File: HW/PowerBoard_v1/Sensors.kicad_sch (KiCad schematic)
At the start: 4 parts, among them U1 AMC130M02DFMR, U1 MCP9700AT-ETT, U5 AMC130M02DFMR

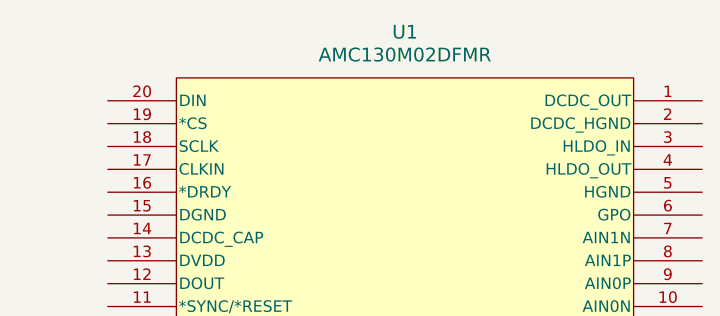
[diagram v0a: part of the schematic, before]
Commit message: cleaned up schematic
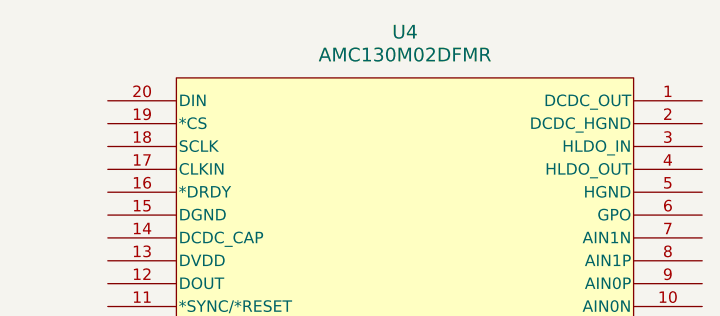
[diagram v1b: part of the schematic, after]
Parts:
- renumbered U1 to U4
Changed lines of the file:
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@@
         )
         (path "/1e1b062d-fad0-427c-a622-c5b8a80b5268/f37b00a5-62bb-47d6-b18e-0a47b6349fc3"
-          (reference "#PWR03") (unit 1)
+          (reference "#PWR017") (unit 1)
         )
       )
@@
         )
         (path "/1e1b062d-fad0-427c-a622-c5b8a80b5268/f37b00a5-62bb-47d6-b18e-0a47b6349fc3"
-          (reference "U4") (unit 1)
+          (reference "U3") (unit 1)
         )
       )
@@
   (symbol (lib_id "AMC130M02DFMR:AMC130M02DFMR") (at 109.22 43.18 0) (unit 1)
     (in_bom yes) (on_board yes) (dnp no) (fields_autoplaced)
-    (property "Reference" "U1" (at 140.97 31.75 0)
+    (property "Reference" "U4" (at 140.97 31.75 0)
       (effects (font (size 1.524 1.524)))
     )
@@
       (project "power_v1"
         (path "/1e1b062d-fad0-427c-a622-c5b8a80b5268/f37b00a5-62bb-47d6-b18e-0a47b6349fc3"
-          (reference "U1") (unit 1)
+          (reference "U4") (unit 1)
         )
       )
@@
         )
         (path "/1e1b062d-fad0-427c-a622-c5b8a80b5268/f37b00a5-62bb-47d6-b18e-0a47b6349fc3"
-          (reference "#PWR04") (unit 1)
+          (reference "#PWR018") (unit 1)
         )
       )
@@
         )
         (path "/1e1b062d-fad0-427c-a622-c5b8a80b5268/f37b00a5-62bb-47d6-b18e-0a47b6349fc3"
-          (reference "C10") (unit 1)
+          (reference "C9") (unit 1)
         )
       )

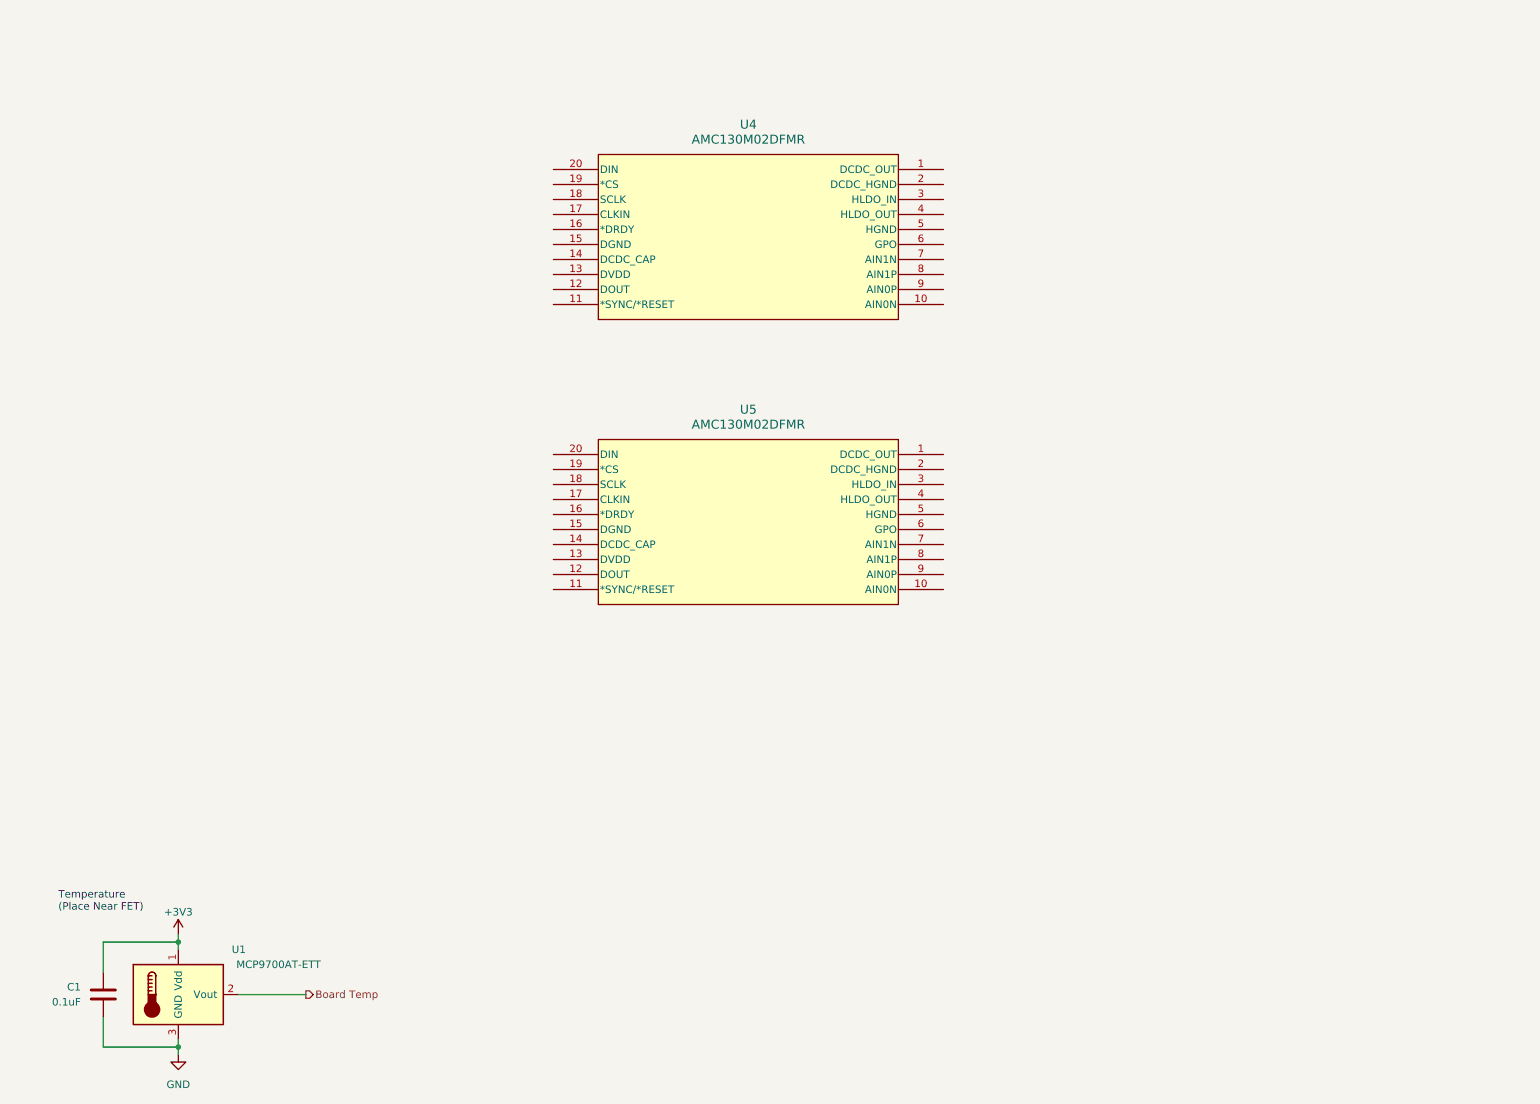
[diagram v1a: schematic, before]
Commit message: update sim to simulate array better
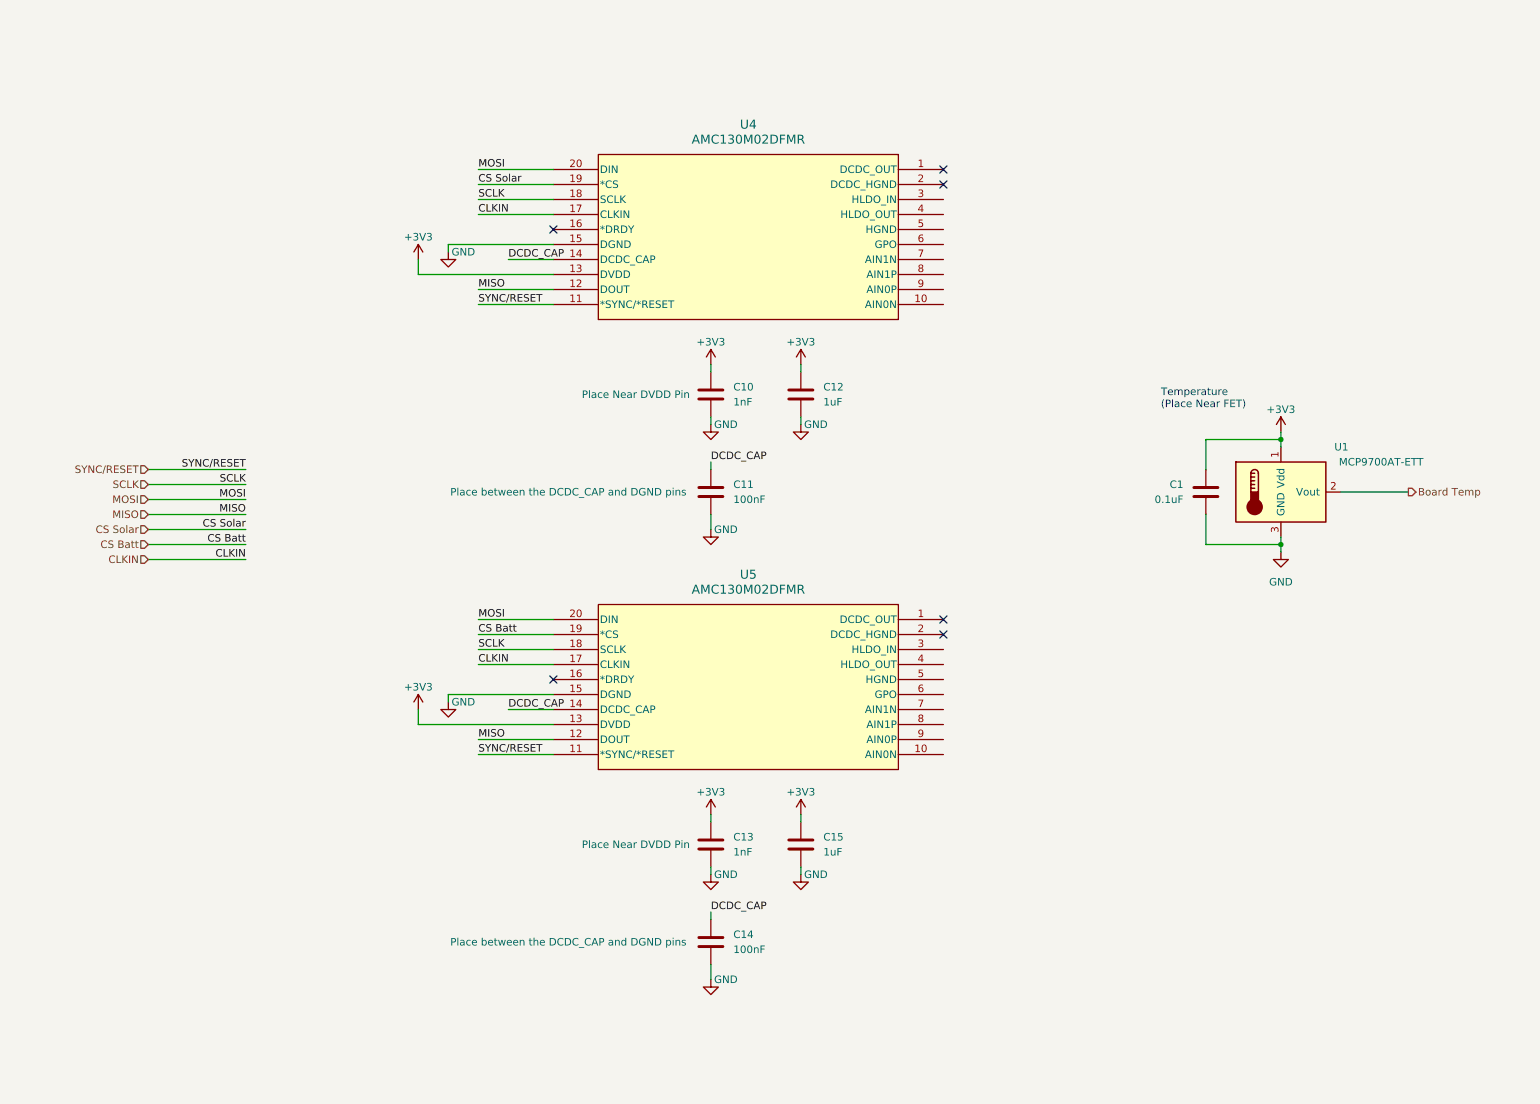
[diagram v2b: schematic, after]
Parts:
- added C10, C13: 1nF, symbol Device:C
- added C11, C14: 100nF, symbol Device:C
- added C12, C15: 1uF, symbol Device:C
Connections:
- net +3V3: now also U4.13 (DVDD), U5.13 (DVDD), C10.1, C12.1, C13.1, C15.1
- net GND: now also U4.15 (DGND), U5.15 (DGND), C10.2, C11.2, C12.2, C13.2, C14.2, C15.2
- net SYNC/RESET: now reaches U4.11 (*SYNC/*RESET)
- net SYNC/RESET: now also U5.11 (*SYNC/*RESET)
- net MISO: now reaches U4.12 (DOUT)
- net MISO: now also U5.12 (DOUT)
- net DCDC_CAP: now reaches U4.14 (DCDC_CAP)
- net DCDC_CAP: now also U5.14 (DCDC_CAP), C11.1, C14.1
- net CLKIN: now reaches U4.17 (CLKIN)
- net CLKIN: now also U5.17 (CLKIN)
- net SCLK: now reaches U4.18 (SCLK)
- net SCLK: now also U5.18 (SCLK)
- net CS Solar: now reaches U4.19 (*CS)
- net MOSI: now reaches U4.20 (DIN)
- net MOSI: now also U5.20 (DIN)
- net CS Batt: now reaches U5.19 (*CS)
- no-connect marks 0 -> 6
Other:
- moved on the sheet: C1, U1

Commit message: updates sensing
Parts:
- removed C10, C13: 1nF, symbol Device:C
- removed C11, C14: 100nF, symbol Device:C
- removed C12, C15: 1uF, symbol Device:C
- removed U4, U5: AMC130M02DFMR, SOIC20_DFM_TEX, symbol AMC130M02DFMR:AMC130M02DFMR
- added U4: PAMC1350DWVR, U_PAMC1350DWVR_TEX, symbol AMC1350:PAMC1350DWVR
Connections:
- no-connect marks 6 -> 0

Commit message: updated sensing portion
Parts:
- added C10, C11, C15, C16, C20, C21, C22, C23: 100nF, Capacitor_SMD:C_0603_1608Metric_Pad1.08x0.95mm_HandSolder, symbol device:C
- added C12, C13, C14, C17, C18, C19, C24, C25: 1uF, Capacitor_SMD:C_0603_1608Metric_Pad1.08x0.95mm_HandSolder, symbol device:C
- added C26: 10uF, Capacitor_SMD:C_0603_1608Metric_Pad1.08x0.95mm_HandSolder, symbol device:C
- added C27: 2.2nF, Capacitor_SMD:C_0603_1608Metric_Pad1.08x0.95mm_HandSolder, symbol device:C
- added C28: 1nF, Capacitor_SMD:C_0603_1608Metric_Pad1.08x0.95mm_HandSolder, symbol device:C
- added L3: 22uH, Inductor_SMD:L_0603_1608Metric_Pad1.05x0.95mm_HandSolder, symbol device:L
- added TP1: +3V3A, TestPoint:TestPoint_THTPad_1.0x1.0mm_Drill0.5mm, symbol Connector:TestPoint
- added TP2: GNDA, TestPoint:TestPoint_THTPad_1.0x1.0mm_Drill0.5mm, symbol Connector:TestPoint
- added U5, U6, U7: PAMC1350DWVR, U_PAMC1350DWVR_TEX, symbol AMC1350:PAMC1350DWVR
- added U8: 3v3 ISO DC/DC, Converter_DCDC:Converter_DCDC_RECOM_R-78S-0.1_THT, symbol Regulator_Switching:CRE1S0305S3C
- U4: MPN (none) -> PAMC1350DWVR
- renumbered C1 to C9, U1 to U3
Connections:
- net +3V3: now also U4.8 (VDD2), C10.1, C12.1, C16.1, C17.1, C22.1, C23.1, C24.1, C25.1, C26.1, L3.1, U5.8 (VDD2), U6.8 (VDD2), U7.8 (VDD2)
- net GND: now also U4.5 (GND2), U4.6 (OUTN), C10.2, C12.2, C16.2, C17.2, C22.2, C23.2, C24.2, C25.2, C26.2, C27.1, U5.5 (GND2), U5.6 (OUTN), U6.5 (GND2), U6.6 (OUTN), U7.5 (GND2), U7.6 (OUTN), U8.1 (-VIN)
- net +3.3VA: now reaches U4.1 (VDD1)
- net +3.3VA: now also C11.1, C13.1, C14.1, C15.1, C18.1, C19.1, C20.1, C21.1, C28.1, TP1.1, U5.1 (VDD1), U6.1 (VDD1), U7.1 (VDD1), U8.4 (+VOUT)
- net V Sense Sol: now reaches U4.2 (INP)
- net Earth: now reaches U4.3 (INN)
- net Earth: now also U4.4 (GND1), C11.2, C13.2, C14.2, C15.2, C18.2, C19.2, C20.2, C21.2, C27.2, TP2.1, U5.3 (INN), U5.4 (GND1), U6.4 (GND1), U7.4 (GND1), U8.3 (-VOUT)
- net ADC V Sol: now reaches U4.7 (OUTP)
- new net: C28.2, L3.2, U8.2 (+VIN)
- new net ADC I Batt: U7.7 (OUTP)
- new net ADC I Sol: U6.7 (OUTP)
- new net ADC V Batt: U5.7 (OUTP)
- new net I+ Sense Batt: U7.2 (INP)
- new net I+ Sense Sol: U6.2 (INP)
- new net I- Sense Batt: U7.3 (INN)
- new net I- Sense Sol: U6.3 (INN)
- new net V Sense Batt: U5.2 (INP)
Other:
- note added: "+3.3VA represents the High Voltage 3.3v side."
- note added: "HV Side"
- note added: "LV Side"
- moved on the sheet: C9, U3, U4

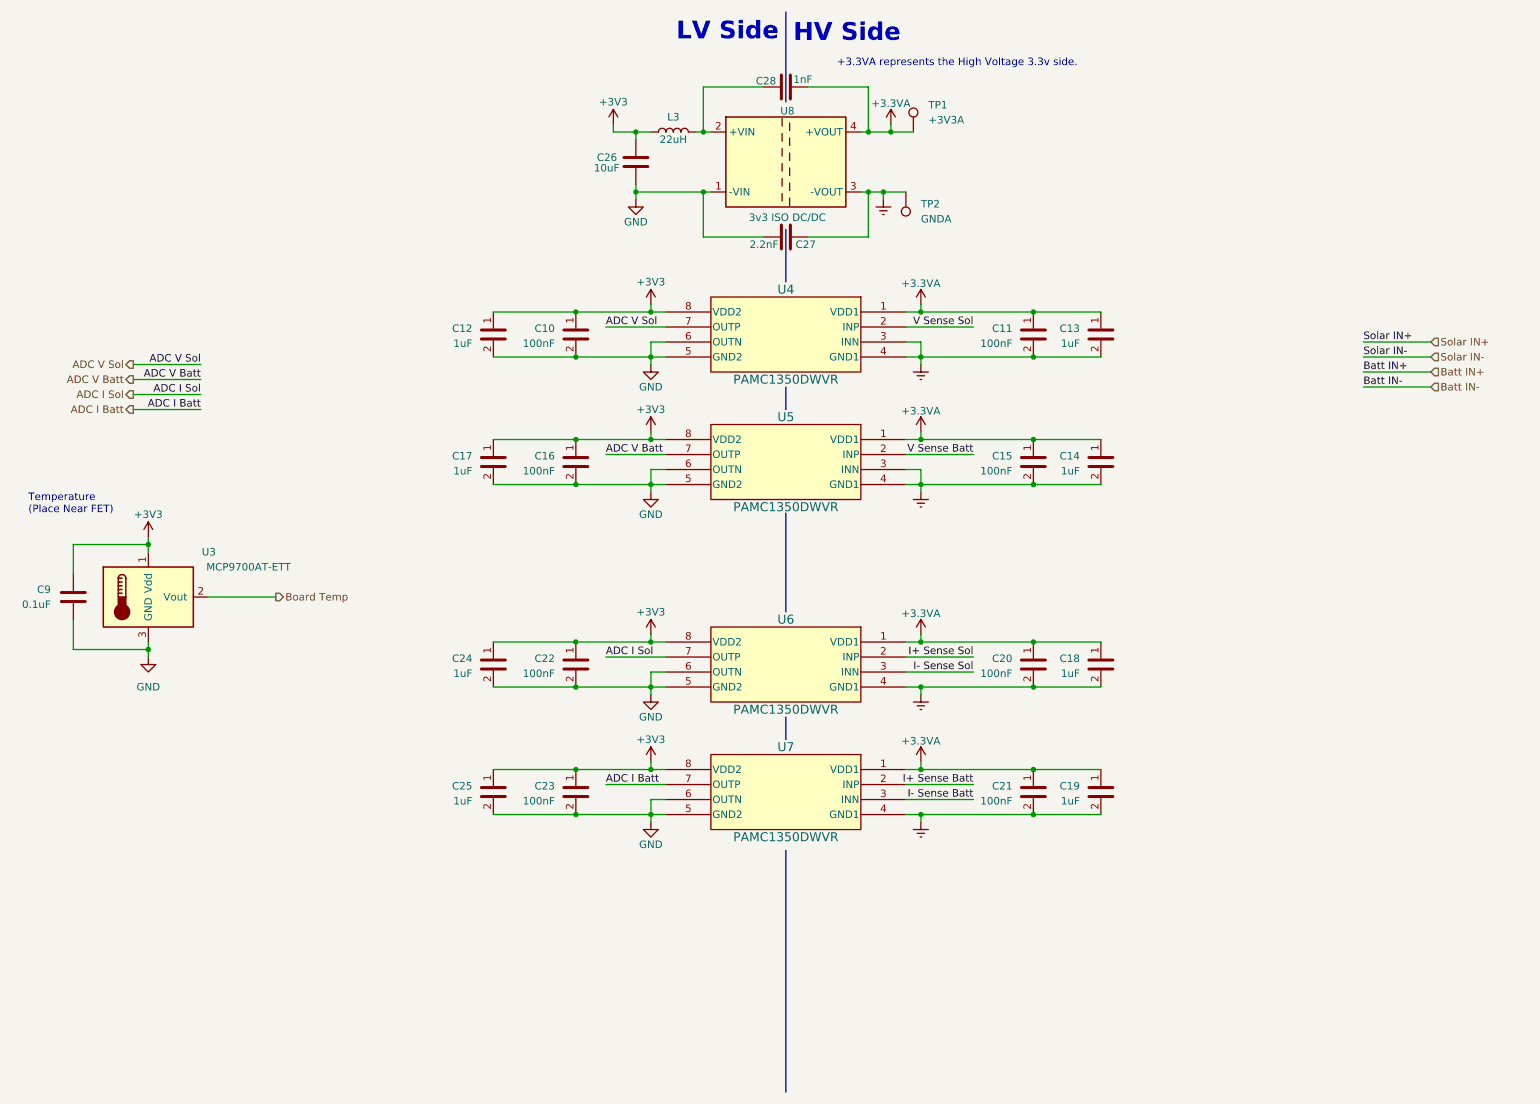
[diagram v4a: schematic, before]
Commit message: added resistors for sensing
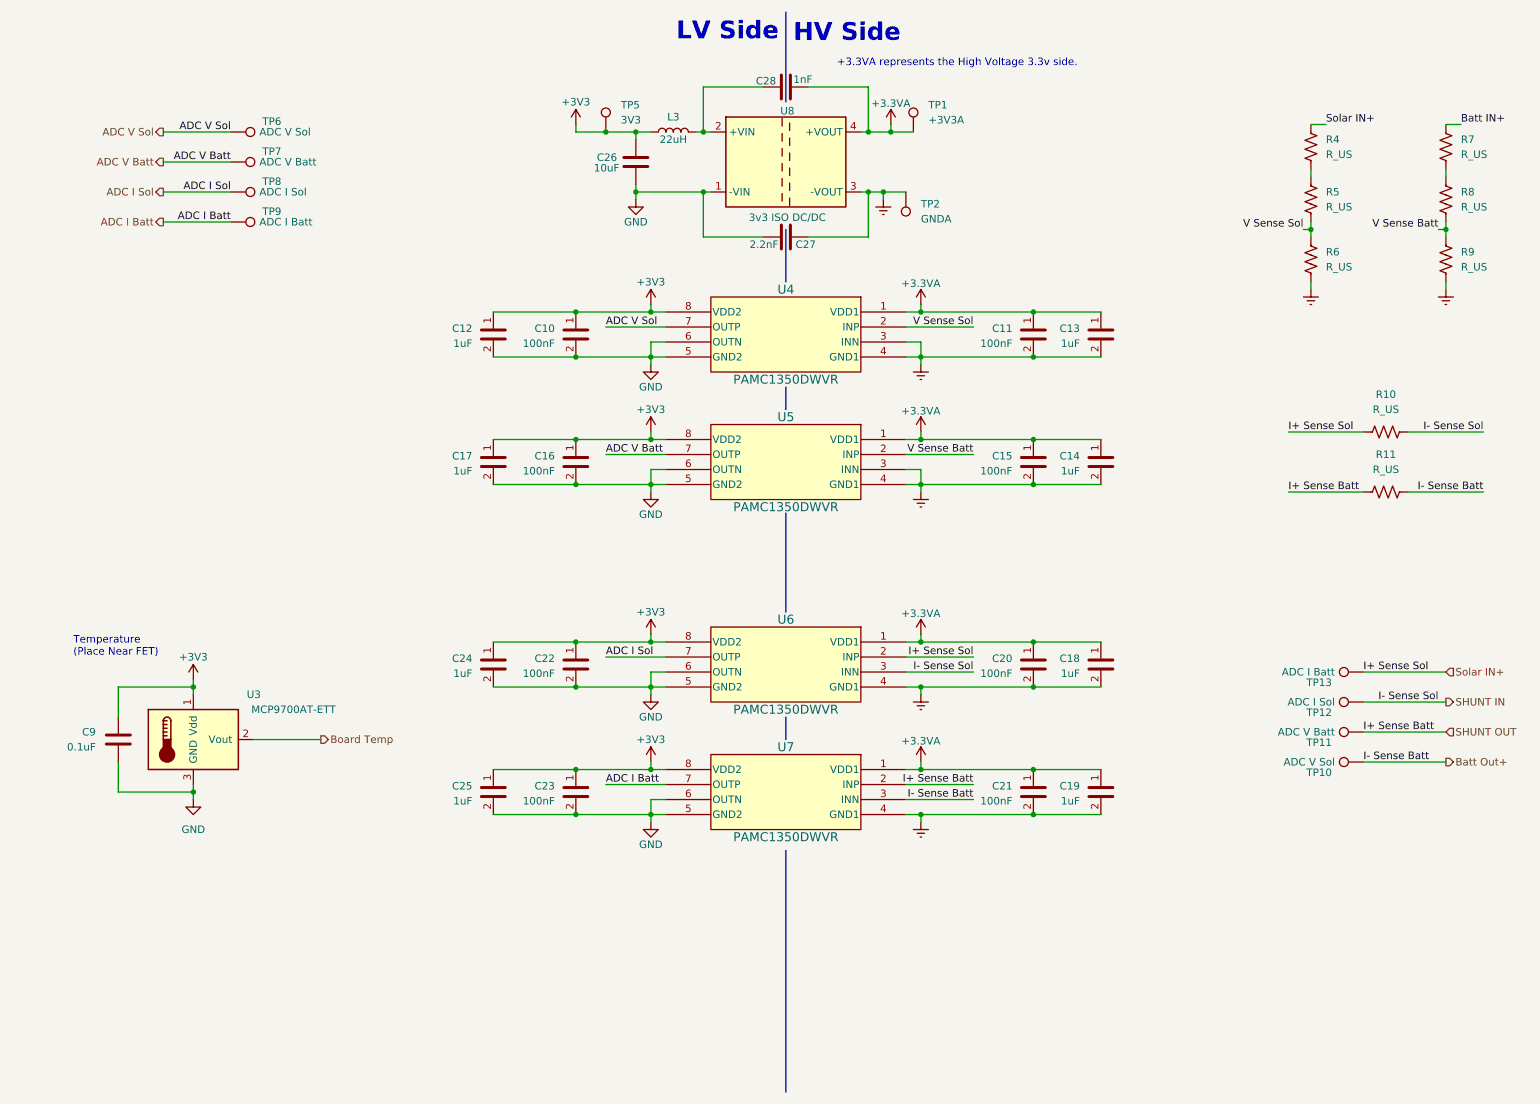
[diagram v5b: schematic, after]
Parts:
- added R10, R11, R4, R5, R6, R7, R8, R9: R_US, symbol device:R_US
- added TP10, TP6: ADC V Sol, TestPoint:TestPoint_THTPad_1.0x1.0mm_Drill0.5mm, symbol Connector:TestPoint
- added TP11, TP7: ADC V Batt, TestPoint:TestPoint_THTPad_1.0x1.0mm_Drill0.5mm, symbol Connector:TestPoint
- added TP12, TP8: ADC I Sol, TestPoint:TestPoint_THTPad_1.0x1.0mm_Drill0.5mm, symbol Connector:TestPoint
- added TP13, TP9: ADC I Batt, TestPoint:TestPoint_THTPad_1.0x1.0mm_Drill0.5mm, symbol Connector:TestPoint
- added TP5: 3V3, TestPoint:TestPoint_THTPad_1.0x1.0mm_Drill0.5mm, symbol Connector:TestPoint
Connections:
- net I+ Sense Sol is gone; now on net Solar IN+: U6.2 (INP)
- net +3V3: now also TP5.1
- net ADC I Batt: now also TP9.1
- net ADC I Sol: now also TP8.1
- net ADC V Batt: now also TP7.1
- net ADC V Sol: now also TP6.1
- net Batt IN+: now also R7.1
- net Earth: now also R6.2, R9.2
- net Solar IN+: now also R10.1, R4.1, TP13.1
- net V Sense Batt: now also R8.2, R9.1
- net V Sense Sol: now also R5.2, R6.1
- net I+ Sense Batt renamed SHUNT OUT
- net SHUNT OUT: now also R11.1, TP11.1
- net I- Sense Batt renamed Batt Out+
- net Batt Out+: now also R11.2, TP10.1
- net I- Sense Sol renamed SHUNT IN
- net SHUNT IN: now also R10.2, TP12.1
- new net: R4.2, R5.1
- new net: R7.2, R8.1
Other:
- moved on the sheet: C9, U3
